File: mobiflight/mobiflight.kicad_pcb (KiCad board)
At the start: 2 copper layers, 66.5 x 104.1 mm, 24 parts, among them J1 Barrel_Jack_Switch, U1 ULN2003, U2 ULN2003, U3 ULN2003, U4 ULN2003, U5 ULN2003, U6 ULN2003

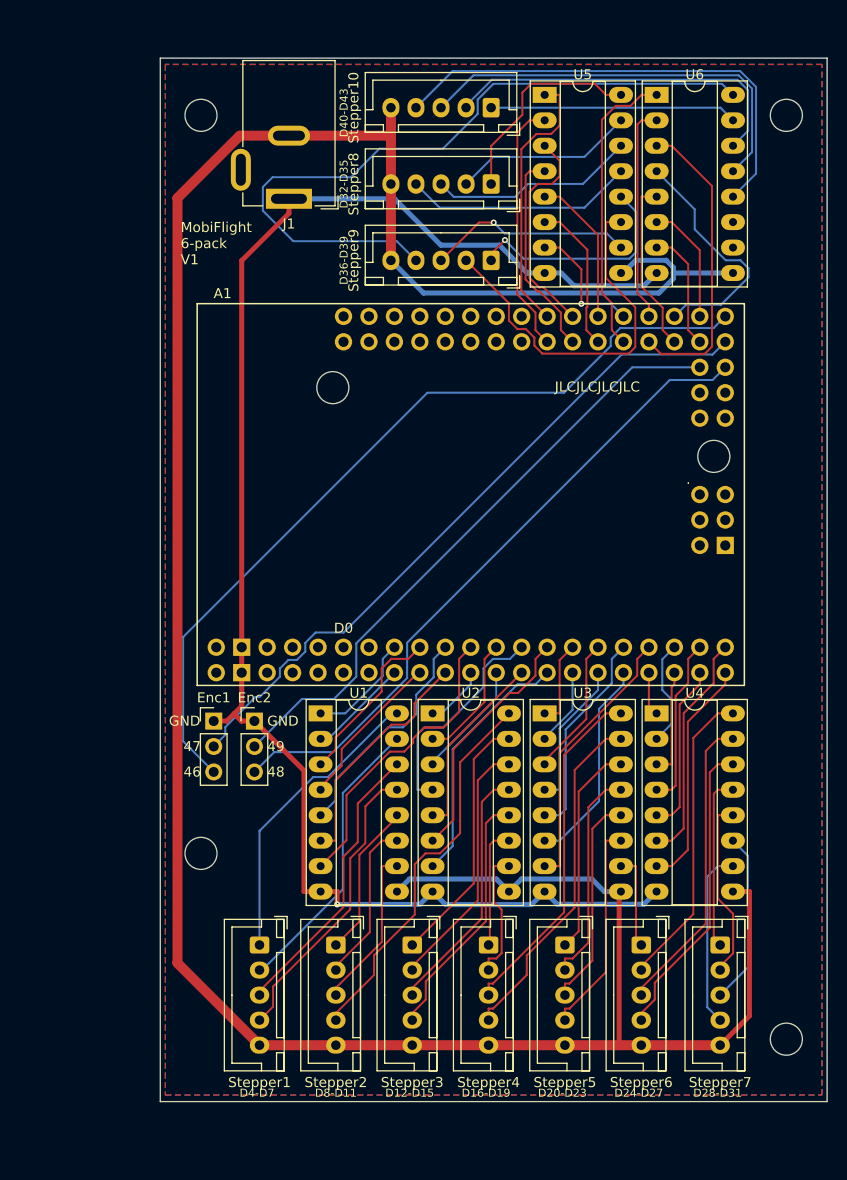
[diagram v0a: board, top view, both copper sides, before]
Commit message: add LEDs, move to SMD
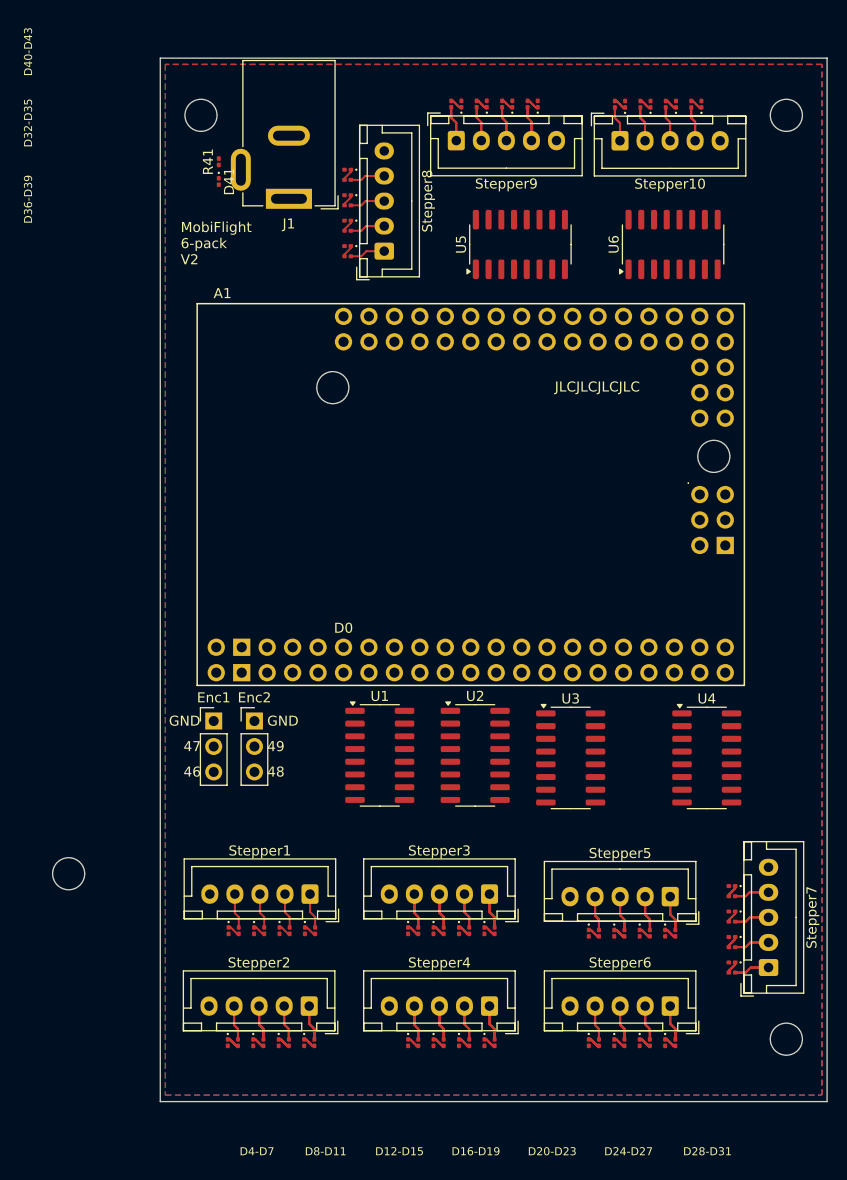
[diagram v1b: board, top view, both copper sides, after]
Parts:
- added D1: LED, LED_SMD:LED_0201_0603Metric, F.Cu at (115.0, 119.2)
- added D10: LED, LED_SMD:LED_0201_0603Metric, F.Cu at (130.4, 119.2)
- added D11: LED, LED_SMD:LED_0201_0603Metric, F.Cu at (127.9, 119.2)
- added D12: LED, LED_SMD:LED_0201_0603Metric, F.Cu at (125.3, 119.2)
- added D13: LED, LED_SMD:LED_0201_0603Metric, F.Cu at (132.9, 130.4)
- added D14: LED, LED_SMD:LED_0201_0603Metric, F.Cu at (130.4, 130.4)
- added D15: LED, LED_SMD:LED_0201_0603Metric, F.Cu at (127.9, 130.4)
- added D16: LED, LED_SMD:LED_0201_0603Metric, F.Cu at (125.3, 130.4)
- added D17: LED, LED_SMD:LED_0201_0603Metric, F.Cu at (151.0, 119.5)
- added D18: LED, LED_SMD:LED_0201_0603Metric, F.Cu at (148.4, 119.5)
- added D19: LED, LED_SMD:LED_0201_0603Metric, F.Cu at (145.9, 119.5)
- added D2: LED, LED_SMD:LED_0201_0603Metric, F.Cu at (112.5, 119.2)
- added D20: LED, LED_SMD:LED_0201_0603Metric, F.Cu at (143.3, 119.5)
- added D21: LED, LED_SMD:LED_0201_0603Metric, F.Cu at (151.0, 130.4)
- added D22: LED, LED_SMD:LED_0201_0603Metric, F.Cu at (148.4, 130.4)
- added D23: LED, LED_SMD:LED_0201_0603Metric, F.Cu at (145.9, 130.4)
- added D24: LED, LED_SMD:LED_0201_0603Metric, F.Cu at (143.3, 130.4)
- added D25: LED, LED_SMD:LED_0201_0603Metric, F.Cu at (157.6, 122.4)
- added D26: LED, LED_SMD:LED_0201_0603Metric, F.Cu at (157.6, 119.8)
- added D27: LED, LED_SMD:LED_0201_0603Metric, F.Cu at (157.6, 117.3)
- added D28: LED, LED_SMD:LED_0201_0603Metric, F.Cu at (157.6, 114.8)
- added D29: LED, LED_SMD:LED_0201_0603Metric, F.Cu at (119.3, 50.9)
- added D3: LED, LED_SMD:LED_0201_0603Metric, F.Cu at (109.9, 119.2)
- added D30: LED, LED_SMD:LED_0201_0603Metric, F.Cu at (119.3, 48.4)
- added D31: LED, LED_SMD:LED_0201_0603Metric, F.Cu at (119.3, 45.8)
- added D32: LED, LED_SMD:LED_0201_0603Metric, F.Cu at (119.3, 43.3)
- added D33: LED, LED_SMD:LED_0201_0603Metric, F.Cu at (130.6, 36.7)
- added D34: LED, LED_SMD:LED_0201_0603Metric, F.Cu at (133.2, 36.7)
- added D35: LED, LED_SMD:LED_0201_0603Metric, F.Cu at (135.7, 36.7)
- added D36: LED, LED_SMD:LED_0201_0603Metric, F.Cu at (138.3, 36.7)
- added D37: LED, LED_SMD:LED_0201_0603Metric, F.Cu at (147.0, 36.7)
- added D38: LED, LED_SMD:LED_0201_0603Metric, F.Cu at (149.5, 36.7)
- added D39: LED, LED_SMD:LED_0201_0603Metric, F.Cu at (152.1, 36.7)
- added D4: LED, LED_SMD:LED_0201_0603Metric, F.Cu at (107.4, 119.2)
- added D40: LED, LED_SMD:LED_0201_0603Metric, F.Cu at (154.6, 36.7)
- added D41: LED, LED_SMD:LED_0201_0603Metric, F.Cu at (106.4, 44.5)
- added D5: LED, LED_SMD:LED_0201_0603Metric, F.Cu at (114.9, 130.4)
- added D6: LED, LED_SMD:LED_0201_0603Metric, F.Cu at (112.4, 130.4)
- added D7: LED, LED_SMD:LED_0201_0603Metric, F.Cu at (109.9, 130.4)
- added D8: LED, LED_SMD:LED_0201_0603Metric, F.Cu at (107.3, 130.4)
- added D9: LED, LED_SMD:LED_0201_0603Metric, F.Cu at (132.9, 119.2)
- added R1: 470R, Resistor_SMD:R_0201_0603Metric, F.Cu at (116.0, 119.2)
- added R10: 470R, Resistor_SMD:R_0201_0603Metric, F.Cu at (131.4, 119.2)
- added R11: 470R, Resistor_SMD:R_0201_0603Metric, F.Cu at (128.9, 119.2)
- added R12: 470R, Resistor_SMD:R_0201_0603Metric, F.Cu at (126.3, 119.2)
- added R13: 470R, Resistor_SMD:R_0201_0603Metric, F.Cu at (134.0, 130.4)
- added R14: 470R, Resistor_SMD:R_0201_0603Metric, F.Cu at (131.4, 130.4)
- added R15: 470R, Resistor_SMD:R_0201_0603Metric, F.Cu at (128.9, 130.4)
- added R16: 470R, Resistor_SMD:R_0201_0603Metric, F.Cu at (126.3, 130.4)
- added R17: 470R, Resistor_SMD:R_0201_0603Metric, F.Cu at (152.0, 119.5)
- added R18: 470R, Resistor_SMD:R_0201_0603Metric, F.Cu at (149.4, 119.5)
- added R19: 470R, Resistor_SMD:R_0201_0603Metric, F.Cu at (146.9, 119.5)
- added R2: 470R, Resistor_SMD:R_0201_0603Metric, F.Cu at (113.5, 119.2)
- added R20: 470R, Resistor_SMD:R_0201_0603Metric, F.Cu at (144.4, 119.5)
- added R21: 470R, Resistor_SMD:R_0201_0603Metric, F.Cu at (152.0, 130.4)
- added R22: 470R, Resistor_SMD:R_0201_0603Metric, F.Cu at (149.4, 130.4)
- added R23: 470R, Resistor_SMD:R_0201_0603Metric, F.Cu at (146.9, 130.4)
- added R24: 470R, Resistor_SMD:R_0201_0603Metric, F.Cu at (144.4, 130.4)
- added R25: 470R, Resistor_SMD:R_0201_0603Metric, F.Cu at (157.6, 123.4)
- added R26: 470R, Resistor_SMD:R_0201_0603Metric, F.Cu at (157.6, 120.9)
- added R27: 470R, Resistor_SMD:R_0201_0603Metric, F.Cu at (157.6, 118.3)
- added R28: 470R, Resistor_SMD:R_0201_0603Metric, F.Cu at (157.6, 115.8)
- added R29: 470R, Resistor_SMD:R_0201_0603Metric, F.Cu at (119.3, 51.9)
- added R3: 470R, Resistor_SMD:R_0201_0603Metric, F.Cu at (111.0, 119.2)
- added R30: 470R, Resistor_SMD:R_0201_0603Metric, F.Cu at (119.3, 49.4)
- added R31: 470R, Resistor_SMD:R_0201_0603Metric, F.Cu at (119.3, 46.8)
- added R32: 470R, Resistor_SMD:R_0201_0603Metric, F.Cu at (119.3, 44.3)
- added R33: 470R, Resistor_SMD:R_0201_0603Metric, F.Cu at (129.6, 36.7)
- added R34: 470R, Resistor_SMD:R_0201_0603Metric, F.Cu at (132.2, 36.7)
- added R35: 470R, Resistor_SMD:R_0201_0603Metric, F.Cu at (134.7, 36.7)
- added R36: 470R, Resistor_SMD:R_0201_0603Metric, F.Cu at (137.2, 36.7)
- added R37: 470R, Resistor_SMD:R_0201_0603Metric, F.Cu at (146.0, 36.7)
- added R38: 470R, Resistor_SMD:R_0201_0603Metric, F.Cu at (148.5, 36.7)
- added R39: 470R, Resistor_SMD:R_0201_0603Metric, F.Cu at (151.0, 36.7)
- added R4: 470R, Resistor_SMD:R_0201_0603Metric, F.Cu at (108.4, 119.2)
- added R40: 470R, Resistor_SMD:R_0201_0603Metric, F.Cu at (153.6, 36.7)
- added R41: 470R, Resistor_SMD:R_0201_0603Metric, F.Cu at (106.4, 42.5)
- added R5: 470R, Resistor_SMD:R_0201_0603Metric, F.Cu at (116.0, 130.4)
- added R6: 470R, Resistor_SMD:R_0201_0603Metric, F.Cu at (113.4, 130.4)
- added R7: 470R, Resistor_SMD:R_0201_0603Metric, F.Cu at (110.9, 130.4)
- added R8: 470R, Resistor_SMD:R_0201_0603Metric, F.Cu at (108.3, 130.4)
- added R9: 470R, Resistor_SMD:R_0201_0603Metric, F.Cu at (134.0, 119.2)
- U1, U2, U3, U4, U5, U6: footprint Package_DIP:DIP-16_W7.62mm_Socket_LongPads -> Package_SO:SOIC-16_3.9x9.9mm_P1.27mm
- moved U5 15.1 mm to (136.5, 50.7), turned to 90 degrees
- moved U6 15.0 mm to (151.8, 50.7), turned to 90 degrees
- moved H2 13.4 mm to (91.4, 113.5)
- moved Stepper10 13.3 mm to (146.5, 40.4), turned to 0 degrees
- moved Stepper8 12.6 mm to (122.9, 51.4), turned to 90 degrees
- moved Stepper9 12.5 mm to (130.1, 40.4), turned to 0 degrees
- moved Stepper5 11.6 mm to (151.5, 115.8), turned to 180 degrees
- moved Stepper3 9.24 mm to (133.4, 115.6), turned to 180 degrees
- moved U1 7.24 mm to (122.5, 101.7)
- moved Stepper1 7.16 mm to (115.5, 115.6), turned to 180 degrees
- moved Stepper6 6.75 mm to (151.5, 126.7), turned to 180 degrees
- moved U4 6.70 mm to (155.1, 102.0)
- moved Stepper2 6.65 mm to (115.5, 126.7), turned to 180 degrees
- moved Stepper4 6.10 mm to (133.4, 126.7), turned to 180 degrees
- moved U2 5.97 mm to (132.0, 101.7)
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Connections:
- J1 pad 1: GND -> VCC
- J1 pad 2: VCC -> GND
- Stepper1 pad 1: S1_1 -> S2_1
- Stepper1 pad 2: S1_2 -> S2_2
- Stepper1 pad 3: S1_3 -> S2_3
- Stepper1 pad 4: S1_4 -> S2_4
- Stepper2 pad 1: S2_1 -> S1_1
- Stepper2 pad 2: S2_2 -> S1_2
- Stepper2 pad 3: S2_3 -> S1_3
- Stepper2 pad 4: S2_4 -> S1_4
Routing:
- net VCC: track 274.3 -> 0.00 mm
- net GND: track 157.3 -> 0.00 mm, vias 1 -> 0
- net Net-(Enc1-Pin_3): track 82.6 -> 0.00 mm
- net Net-(Enc1-Pin_2): track 69.2 -> 0.00 mm
- net Net-(Enc2-Pin_3): track 65.8 -> 0.00 mm
- net S9_4: track 72.2 -> 6.98 mm
- net Net-(Enc2-Pin_2): track 62.1 -> 0.00 mm
- net S10_4: track 48.0 -> 6.98 mm
- net S2_4: track 38.6 -> 3.49 mm
- net S10_3: track 42.0 -> 7.01 mm
- net S9_2: track 37.7 -> 7.04 mm
- net /D41: track 30.3 -> 0.00 mm
- net /D10: track 30.0 -> 0.00 mm
- net /D39: track 29.5 -> 0.00 mm
- net S10_2: track 36.0 -> 7.04 mm
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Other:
- board text added: "MobiFlight 6-pack V2"
- board text removed: "MobiFlight 6-pack V1"

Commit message: replace components
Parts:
- moved Enc1 65.9 mm to (161.5, 63.0), turned to 180 degrees
- moved Enc2 57.4 mm to (161.5, 73.2), turned to 180 degrees
- moved H2 22.4 mm to (105.4, 131.1)
- moved D2 16.4 mm to (116.7, 114.1)
- moved D3 16.4 mm to (114.2, 114.1)
- moved D4 16.4 mm to (111.6, 114.1)
- moved R2 16.4 mm to (117.7, 114.1)
- moved R4 16.4 mm to (112.7, 114.1)
- moved R5 16.4 mm to (110.1, 114.1)
- moved D5 16.4 mm to (109.1, 114.1)
- moved R3 16.4 mm to (115.2, 114.1)
- moved Stepper1 16.4 mm to (117.2, 110.5)
- moved R22 16.3 mm to (165.2, 109.0), turned to 180 degrees
- moved D22 14.5 mm to (165.2, 110.0), turned to 0 degrees
- moved Stepper7 13.4 mm to (161.5, 109.5), turned to -90 degrees
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- renumbered D41 to D1, D13 to D10, D14 to D11, D15 to D12, D16 to D13, D17 to D14, D18 to D15, D19 to D16, D20 to D17, D21 to D18, D22 to D19, D5 to D2, D23 to D20, D24 to D21, D25 to D22, D26 to D23, D27 to D24, D28 to D25, D29 to D26, D30 to D27, D31 to D28, D32 to D29, D6 to D3, D33 to D30, D34 to D31, D35 to D32, D36 to D33, D37 to D34, D38 to D35, D39 to D36, D40 to D37, D1 to D38, D2 to D39, D7 to D4, D3 to D40, D4 to D41, D8 to D5, D9 to D6, D10 to D7, D11 to D8, D12 to D9, R41 to R1, R13 to R10, R14 to R11, R15 to R12, R16 to R13, R17 to R14, R18 to R15, R19 to R16, R20 to R17, R21 to R18, R22 to R19, R5 to R2, R23 to R20, R24 to R21, R25 to R22, R26 to R23, R27 to R24, R28 to R25, R29 to R26, R30 to R27, R31 to R28, R32 to R29, R6 to R3, R33 to R30, R34 to R31, R35 to R32, R36 to R33, R37 to R34, R38 to R35, R39 to R36, R40 to R37, R1 to R38, R2 to R39, R7 to R4, R3 to R40, R4 to R41, R8 to R5, R9 to R6, R10 to R7, R11 to R8, R12 to R9, Stepper2 to Stepper1, Stepper1 to Stepper2
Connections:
- net /D14 renamed D14
- net /D21 renamed D21
- net /D28 renamed D28
- net /D32 renamed D32
- net /D33 renamed D33
- net /D34 renamed D34
- net /D35 renamed D35
- net /D36 renamed D36
- net /D37 renamed D37
- net /D38 renamed D38
- net /D39 renamed D39
- net /D40 renamed D40
- net /D41 renamed D41
- net /D42 renamed D42
- net /D43 renamed D43
- net /D44 renamed D44
- net /D45 renamed D45
- net /D7 renamed D7
- A1 pad D10: /D10 -> D10
- A1 pad D11: /D11 -> D11
- A1 pad D12: /D12 -> D12
- A1 pad D13: /D13 -> D13
- A1 pad D15: /D15 -> D15
- A1 pad D16: /D16 -> D16
- A1 pad D17: /D17 -> D17
- A1 pad D18: /D18 -> D18
- A1 pad D19: /D19 -> D19
- A1 pad D20: /D20 -> D20
- A1 pad D22: /D22 -> D22
- A1 pad D23: /D23 -> D23
- A1 pad D24: /D24 -> D24
- A1 pad D25: /D25 -> D25
- A1 pad D26: /D26 -> D26
- A1 pad D27: /D27 -> D27
- A1 pad D29: /D29 -> D29
- A1 pad D30: /D30 -> D30
- A1 pad D31: /D31 -> D31
- A1 pad D4: /D4 -> D4
- A1 pad D49: Net-(Enc2-Pin_2) -> unconnected-(A1-PadD49)
- A1 pad D5: /D5 -> D5
- A1 pad D50: unconnected-(A1-D50_MISO-PadD50) -> Net-(A1-D50_MISO)
- A1 pad D6: /D6 -> D6
- A1 pad D8: /D8 -> D8
- A1 pad D9: /D9 -> D9
- Enc2 pad 2: Net-(Enc2-Pin_2) -> Net-(A1-D50_MISO)
- U1 pad 1: /D4 -> D10
- U1 pad 10: S2_3 -> S1_4
- U1 pad 11: S2_2 -> S1_3
- U1 pad 12: S2_1 -> S1_2
- U1 pad 13: S1_4 -> S1_1
- U1 pad 14: S1_3 -> S2_4
- U1 pad 15: S1_2 -> S2_3
- U1 pad 16: S1_1 -> S2_2
- U1 pad 2: /D5 -> D9
- U1 pad 3: /D6 -> D8
- U1 pad 5: /D8 -> D6
- U1 pad 6: /D9 -> D5
- U1 pad 7: /D10 -> D4
- U2 pad 1: /D11 -> D17
- U2 pad 10: S4_2 -> S2_1
- U2 pad 11: S4_1 -> S3_4
- U2 pad 12: S3_4 -> S3_3
- U2 pad 13: S3_3 -> S3_2
- U2 pad 14: S3_2 -> S3_1
- U2 pad 15: S3_1 -> S4_4
- U2 pad 16: S2_4 -> S4_3
- U2 pad 2: /D12 -> D16
- U2 pad 3: /D13 -> D15
- U2 pad 5: /D15 -> D13
- U2 pad 6: /D16 -> D12
- U2 pad 7: /D17 -> D11
- U3 pad 1: /D18 -> D24
- U3 pad 10: S6_1 -> S4_2
- U3 pad 11: S5_4 -> S4_1
- U3 pad 12: S5_3 -> S5_4
- U3 pad 13: S5_2 -> S5_3
- U3 pad 14: S5_1 -> S5_2
- U3 pad 15: S4_4 -> S5_1
- U3 pad 16: S4_3 -> S6_4
- U3 pad 2: /D19 -> D23
- U3 pad 3: /D20 -> D22
- U3 pad 5: /D22 -> D20
- U3 pad 6: /D23 -> D19
- U3 pad 7: /D24 -> D18
- U4 pad 1: /D25 -> D31
- U4 pad 10: S7_4 -> S6_3
- U4 pad 11: S7_3 -> S6_2
- U4 pad 12: S7_2 -> S6_1
- U4 pad 13: S7_1 -> S7_4
- U4 pad 14: S6_4 -> S7_3
- U4 pad 15: S6_3 -> S7_2
- U4 pad 16: S6_2 -> S7_1
- U4 pad 2: /D26 -> D30
- U4 pad 3: /D27 -> D29
- U4 pad 5: /D29 -> D27
- U4 pad 6: /D30 -> D26
- U4 pad 7: /D31 -> D25
- U5 pad 13: S8_4 -> S8_1
- U5 pad 14: S8_3 -> S8_2
- U5 pad 15: S8_2 -> S8_3
- U5 pad 16: S8_1 -> S8_4
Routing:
- net GND: vias 0 -> 7
- added copper zone on F.Cu, net VCC
- removed copper zone on F.Cu, net GND
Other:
- board text added: "50"
- board text removed: "49"
- board text removed: "D32-D35"
- board text removed: "D36-D39"
- board text removed: "D40-D43"

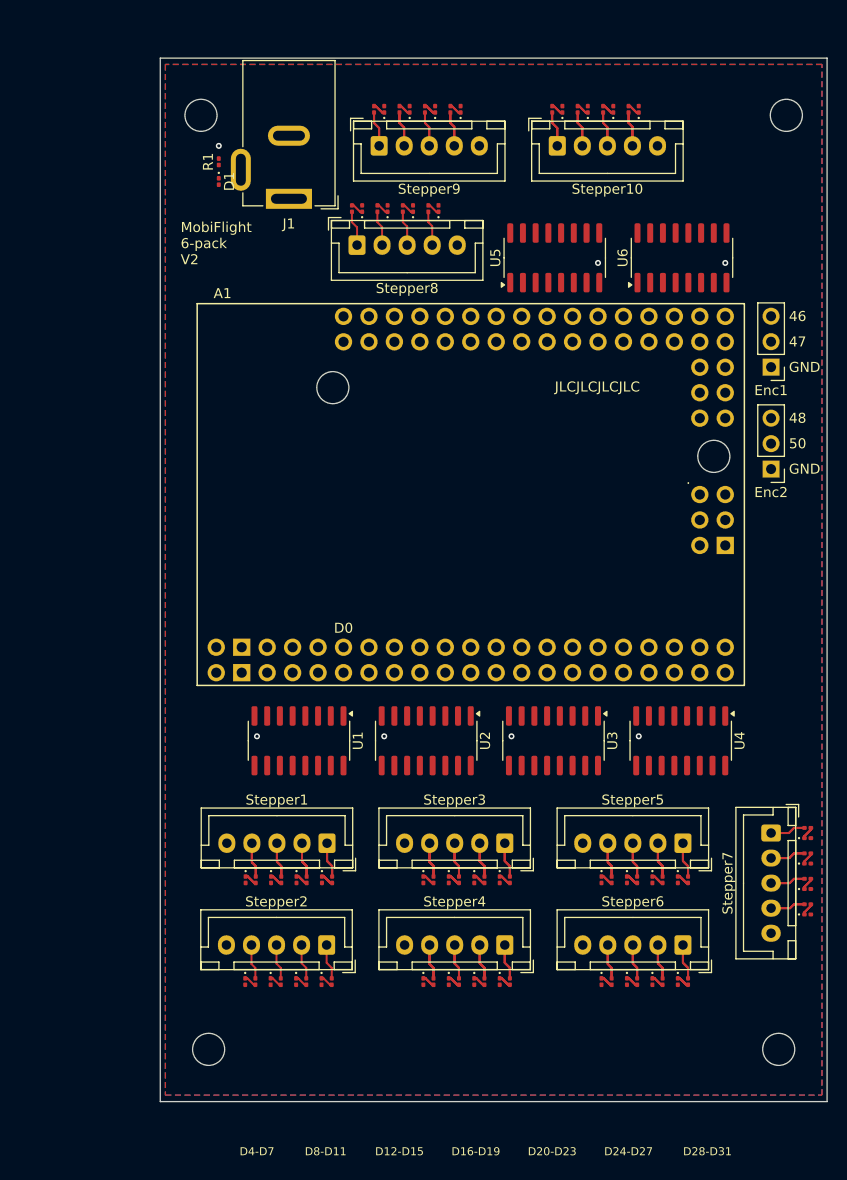
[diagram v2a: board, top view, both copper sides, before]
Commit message: wiring for smd mobiflight
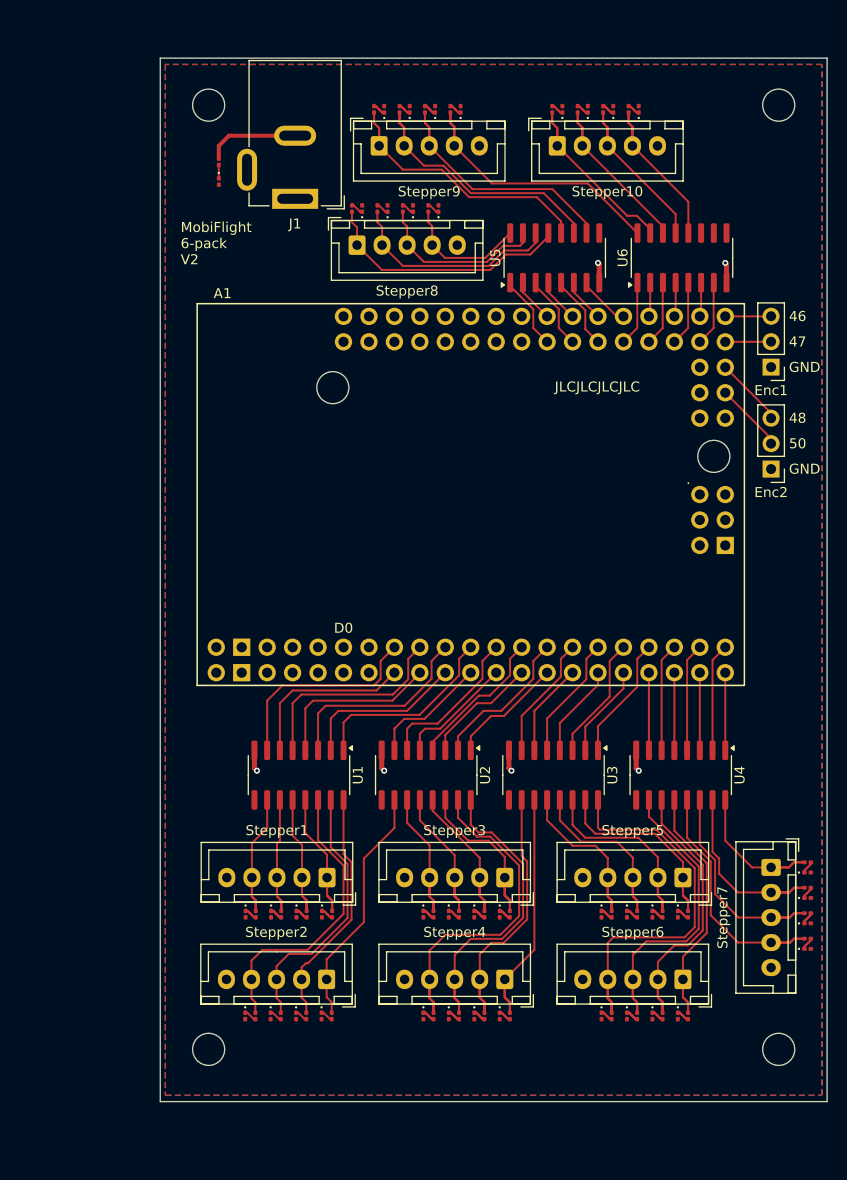
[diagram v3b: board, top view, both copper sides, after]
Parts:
- moved D22 3.43 mm to (165.2, 113.4)
- moved R23 3.43 mm to (165.2, 114.9)
- moved D10 3.43 mm to (134.5, 127.7)
- moved D11 3.43 mm to (131.9, 127.7)
- moved D12 3.43 mm to (129.4, 127.7)
- moved D13 3.43 mm to (126.8, 127.7)
- moved D14 3.43 mm to (152.2, 117.6)
- moved D15 3.43 mm to (149.7, 117.6)
- moved D16 3.43 mm to (147.2, 117.6)
- moved D17 3.43 mm to (144.6, 117.6)
- moved D18 3.43 mm to (152.2, 127.7)
- moved D19 3.43 mm to (149.7, 127.7)
- moved D2 3.43 mm to (116.7, 117.6)
- moved D20 3.43 mm to (147.2, 127.7)
- moved D21 3.43 mm to (144.6, 127.7)
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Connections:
- U5 pad 1: D32 -> D33
- U5 pad 2: D33 -> D32
- U5 pad 3: D34 -> D35
- U5 pad 4: D35 -> D34
- U5 pad 5: D36 -> D37
- U5 pad 6: D37 -> D36
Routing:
- net S6_4: track 10.5 -> 43.4 mm
- net S4_4: track 10.5 -> 38.6 mm
- net S4_3: track 10.5 -> 36.0 mm
- net S2_4: track 3.49 -> 28.9 mm
- net S6_3: track 10.5 -> 35.5 mm
- net S2_3: track 3.50 -> 26.4 mm
- net S9_1: track 7.07 -> 29.5 mm
- net S6_2: track 10.6 -> 32.8 mm
- net GND: track 0.00 -> 21.9 mm, vias 7 -> 6
- net S9_4: track 6.98 -> 28.9 mm
- net S8_1: track 3.54 -> 25.4 mm
- net S9_2: track 7.04 -> 28.1 mm
- net D6: track 0.00 -> 20.9 mm
- net D4: track 0.00 -> 20.9 mm
- net S4_2: track 10.6 -> 31.4 mm
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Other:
- board text added: "S1: 4-7 S2: 8-11 S3: 12-15 S4: 16-19 S5: 20-23 S6: 24-27 S7: 28-31 S8: 32-35 S9: 36-39 S10: 40-43"
- board text removed: "D12-D15"
- board text removed: "D16-D19"
- board text removed: "D20-D23"
- board text removed: "D24-D27"
- board text removed: "D28-D31"
- board text removed: "D4-D7"
- board text removed: "D8-D11"

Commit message: misc
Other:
- board text added: "MobiFlight 6-pack V3"
- board text removed: "MobiFlight 6-pack V2"
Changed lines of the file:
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@@
     (property "ki_keywords" "LED diode")
     (attr smd)
-    (fp_text reference "D1" (at 0 -1.05 90) (layer "F.SilkS") hide
+    (fp_text reference "D1" (at 0 -1.05 -90) (layer "F.SilkS")
         (effects (font (size 1 1) (thickness 0.15)))
     )
-    (fp_text value "LED" (at 0 1.05 90) (layer "F.Fab")
+    (fp_text value "LED" (at 0 1.05 -90) (layer "F.Fab")
         (effects (font (size 1 1) (thickness 0.15)))
     )
-    (fp_text user "${REFERENCE}" (at 0 -0.68 90) (layer "F.Fab")
+    (fp_text user "${REFERENCE}" (at 0 -0.68 -90) (layer "F.Fab")
         (effects (font (size 0.25 0.25) (thickness 0.04)))
     )
@@
     (effects (font (size 1 1) (thickness 0.1)) (justify left))
   )
-  (gr_text "MobiFlight\n6-pack\nV2" (at 102.616 52.832) (layer "F.SilkS")
+  (gr_text "MobiFlight\n6-pack\nV3" (at 102.616 52.832) (layer "F.SilkS")
     (effects (font (size 1 1) (thickness 0.1)) (justify left bottom))
   )
